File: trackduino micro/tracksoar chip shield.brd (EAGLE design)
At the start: 43.7 x 19.6 mm, 5 parts

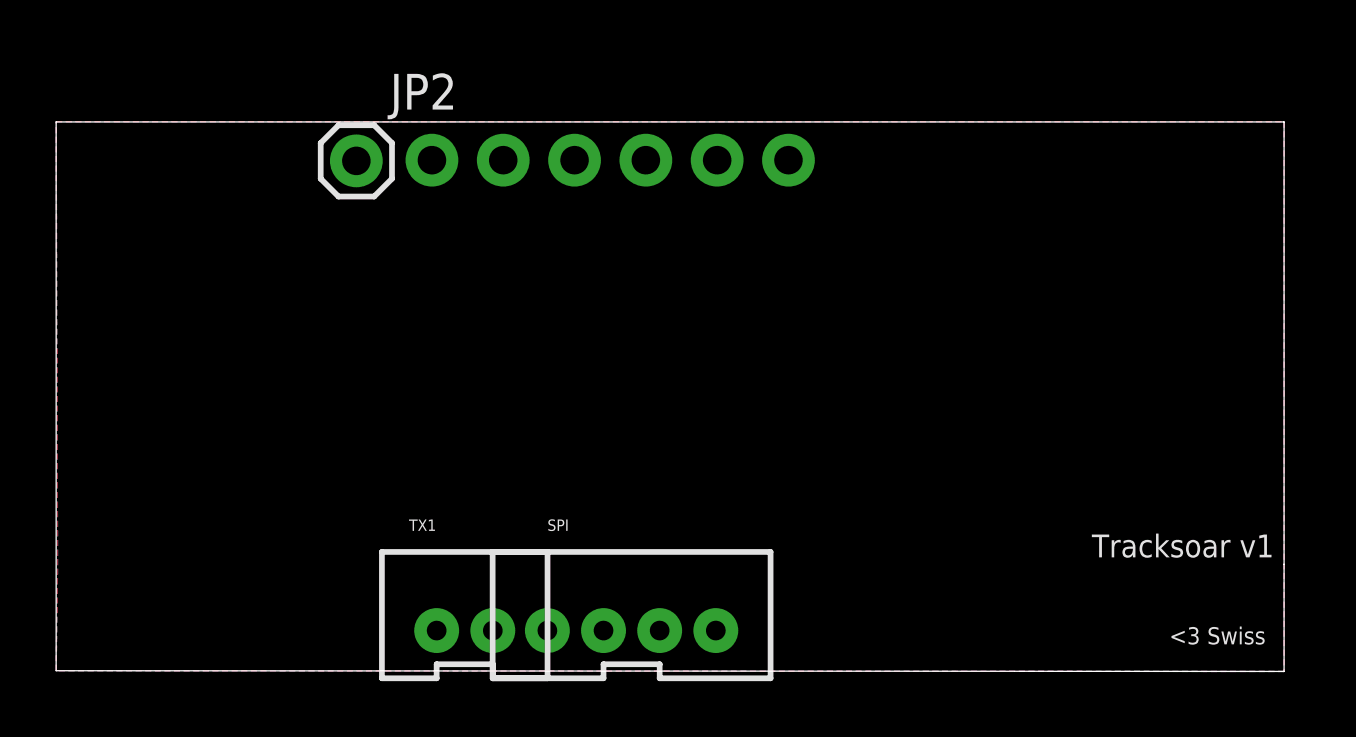
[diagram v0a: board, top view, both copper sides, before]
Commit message: Fixed chip shield
added a cutout to prevent obstructing the GPS chip antenna. Removed an
extra ground trace form the chip board.
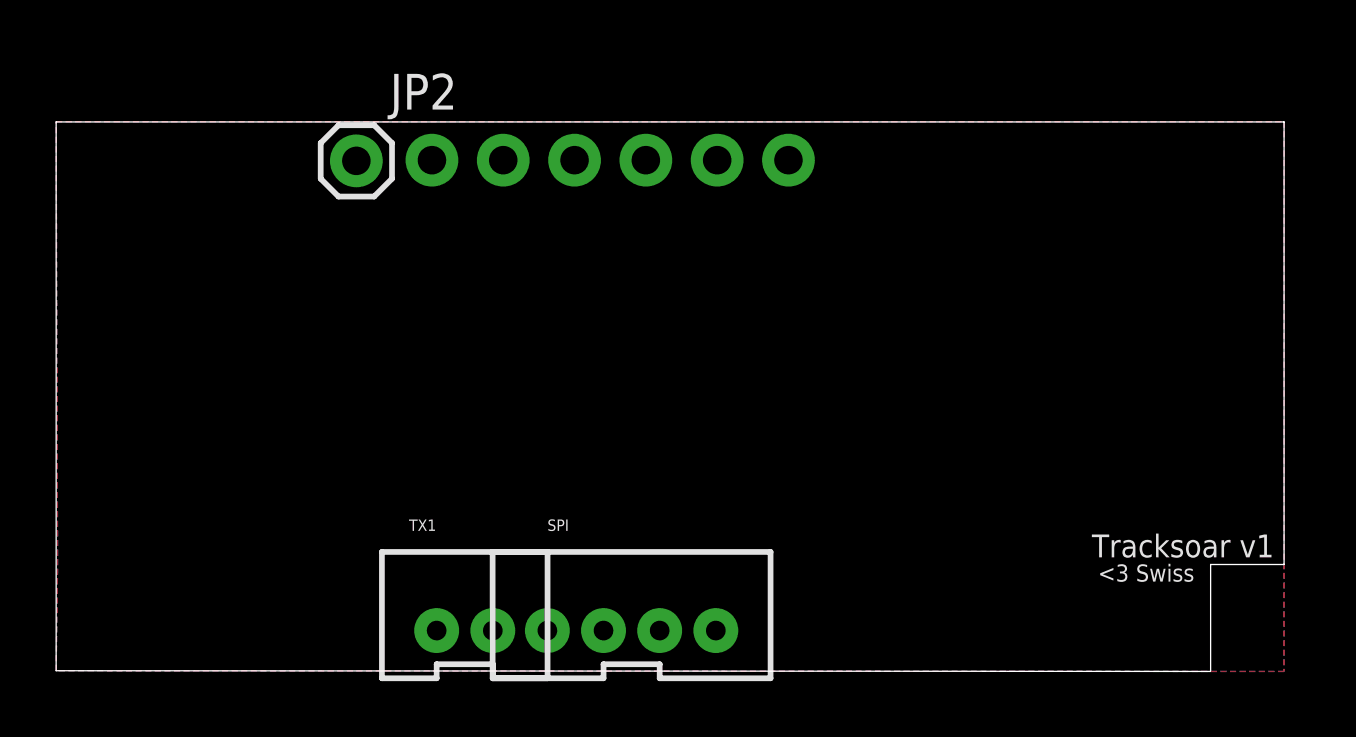
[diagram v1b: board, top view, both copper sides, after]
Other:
- outline, holes or cut-outs redrawn
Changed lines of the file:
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@@
 <board>
 <plain>
-<wire x1="-0.4064" y1="-0.3302" x2="43.3324" y2="-0.3556" width="0" layer="20"/>
-<wire x1="43.3324" y1="-0.3556" x2="43.3324" y2="3.4544" width="0" layer="20"/>
+<wire x1="-0.4064" y1="-0.3302" x2="40.7162" y2="-0.3556" width="0" layer="20"/>
+<wire x1="40.7162" y1="-0.3302" x2="40.7162" y2="3.4544" width="0" layer="20"/>
+<wire x1="40.7162" y1="3.4544" x2="43.3324" y2="3.4544" width="0" layer="20"/>
 <wire x1="43.3324" y1="3.4544" x2="43.3326" y2="19.2178" width="0" layer="20"/>
 <wire x1="43.3326" y1="19.2178" x2="-0.4064" y2="19.2178" width="0" layer="20"/>
 <wire x1="-0.4064" y1="19.2178" x2="-0.4064" y2="-0.3302" width="0" layer="20"/>
 <text x="42.9768" y="4.5212" size="0.8128" layer="25" rot="R180">Tracksoar v1</text>
-<text x="39.243" y="0.6096" size="0.6096" layer="25">&lt;3 Swiss</text>
+<text x="36.703" y="2.8448" size="0.6096" layer="25">&lt;3 Swiss</text>
 </plain>
 <attributes>
@@
 <vertex x="-0.3556" y="3.429"/>
 </polygon>
-<wire x1="23.1394" y1="17.8562" x2="25.6794" y2="17.8562" width="0" layer="19" extent="1-1"/>
 </signal>
 <signal name="VCC">
